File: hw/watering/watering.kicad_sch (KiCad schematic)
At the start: 8 parts, among them J2 USB_C_Receptacle

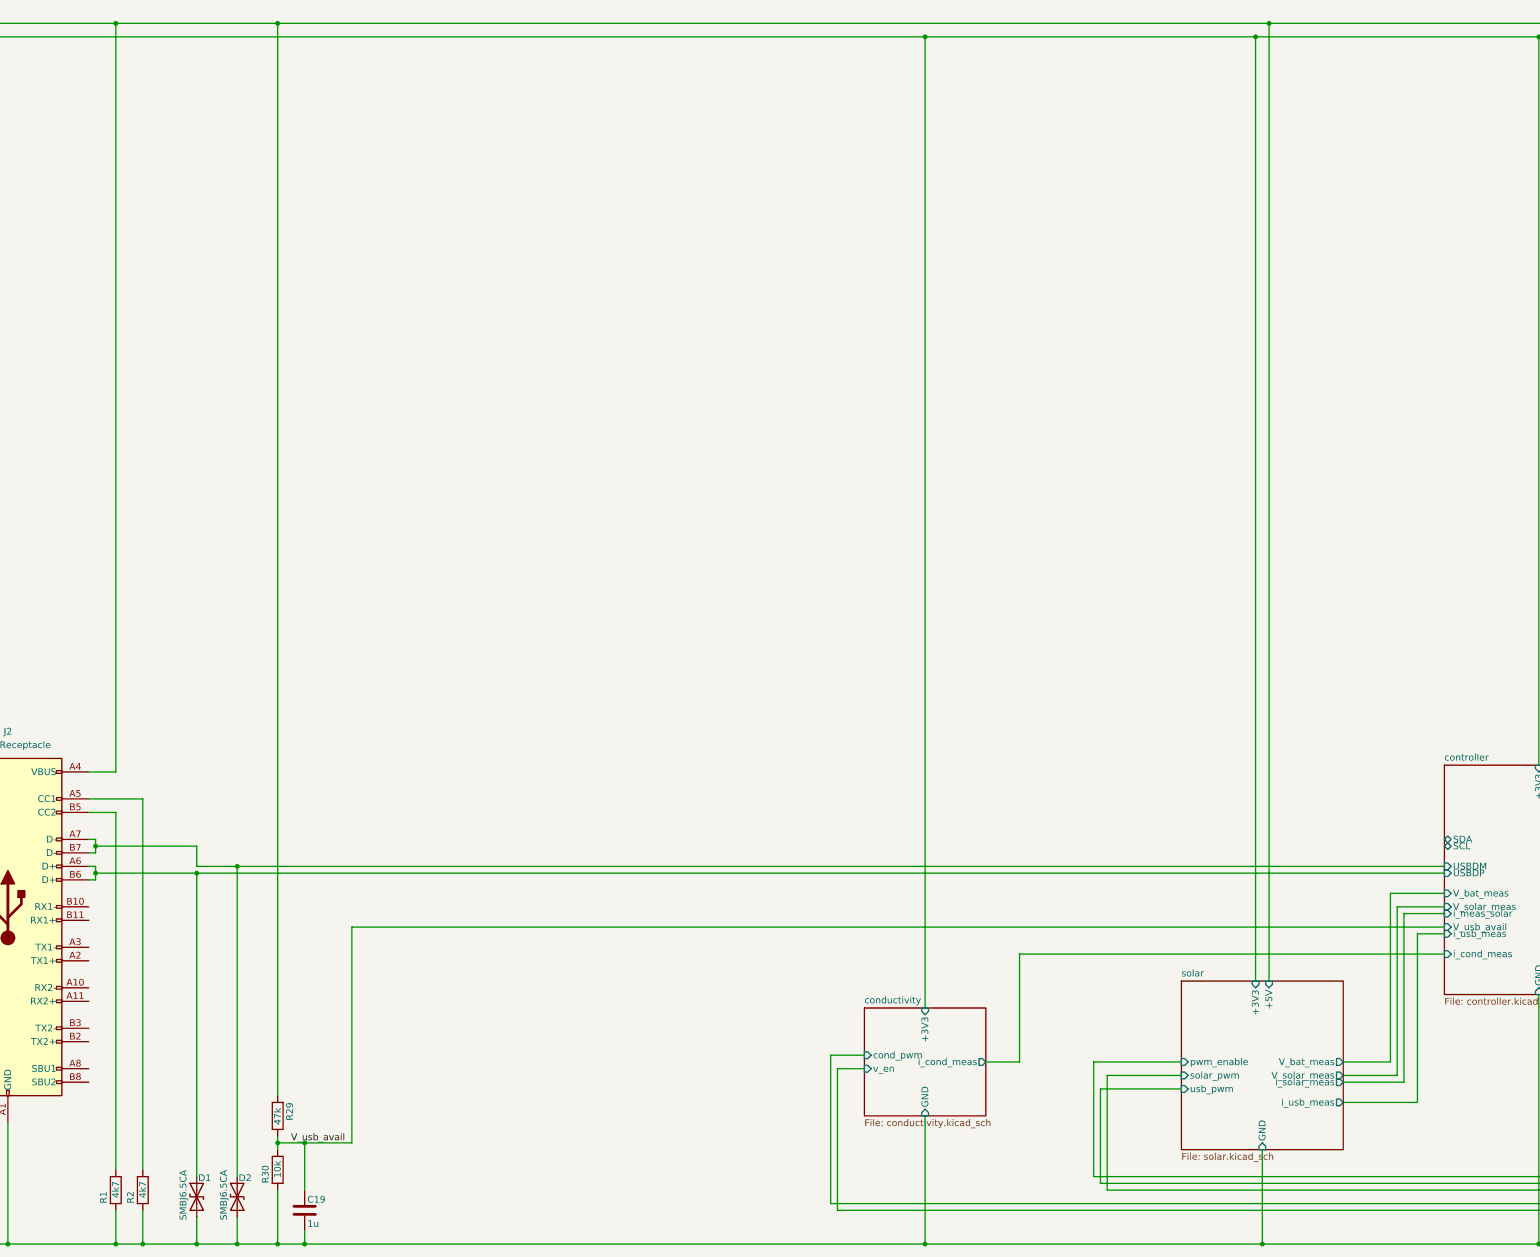
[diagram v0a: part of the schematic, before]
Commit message: more usb compliance
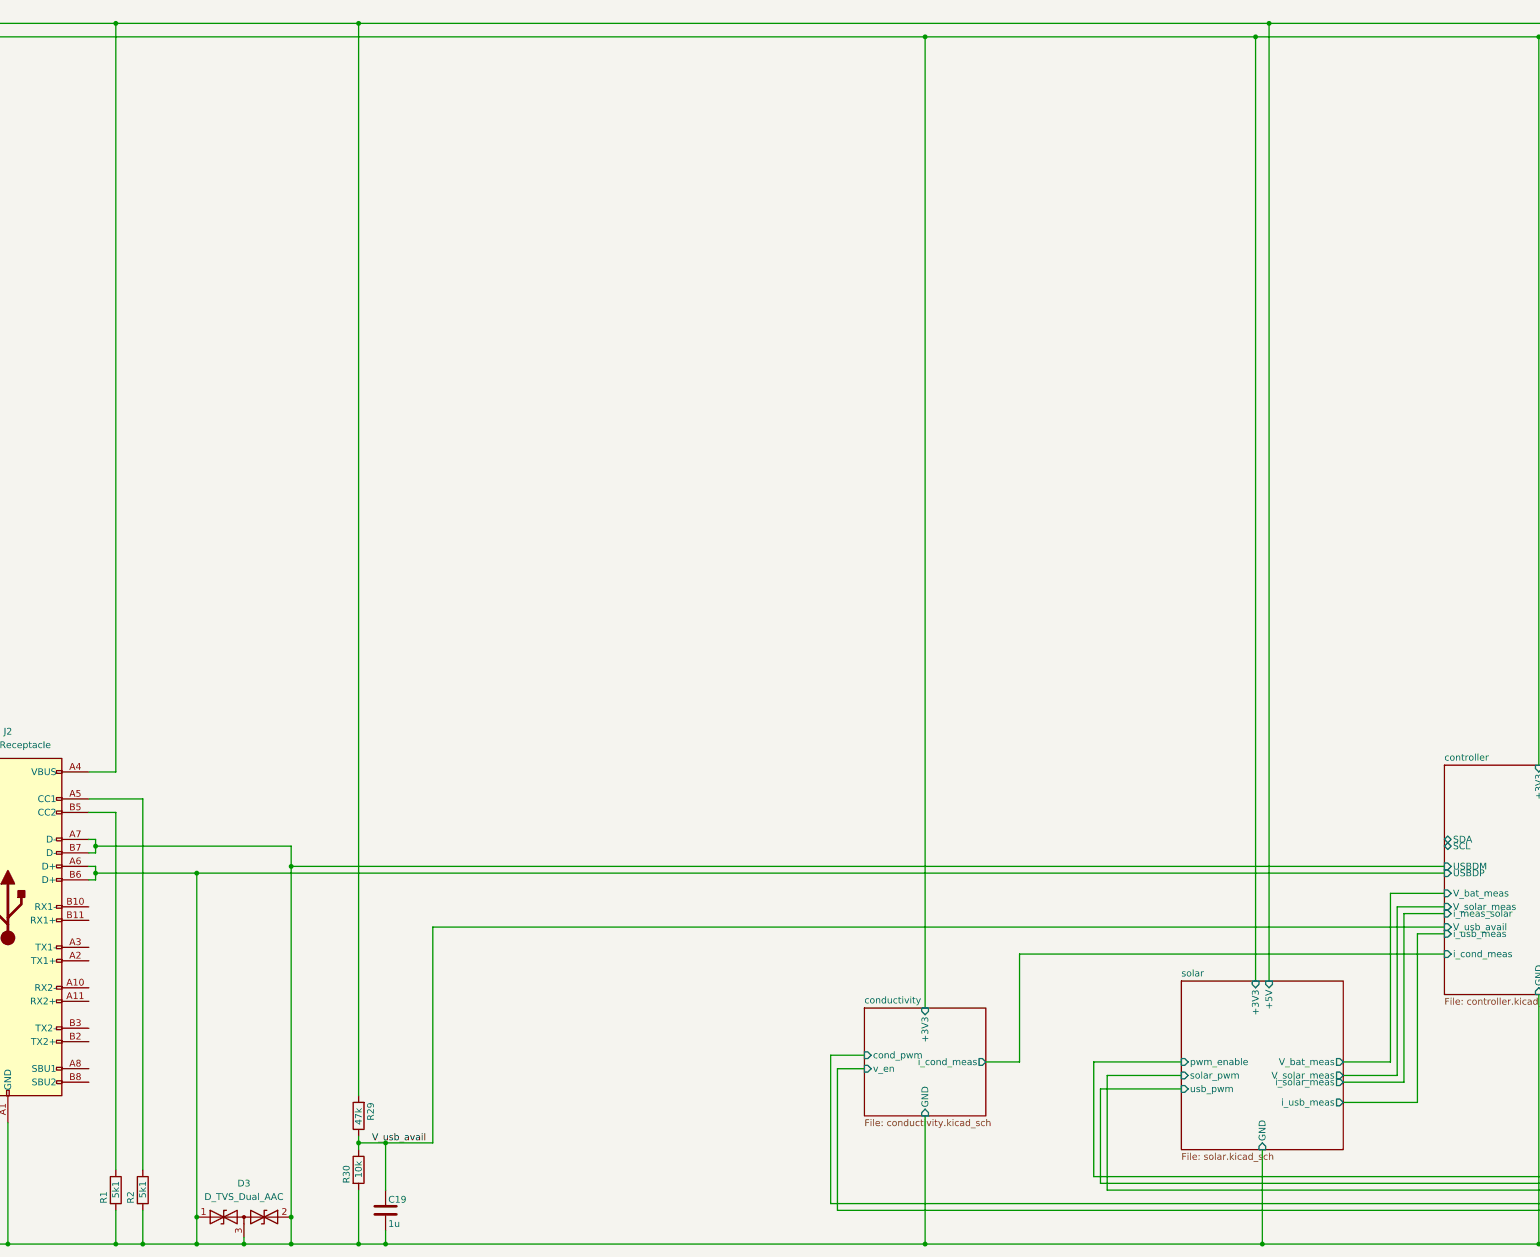
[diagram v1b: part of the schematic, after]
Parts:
- removed D1, D2: SMBJ6.5CA, Diode_SMD:D_SMB, symbol Diode:1N62xxCA
- added D3: D_TVS_Dual_AAC, symbol Device:D_TVS_Dual_AAC
- R1, R2: value 4k7 -> 5k1
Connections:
- net controller/USBDM is gone; now on net GND: J2.A7 (D-), J2.B7 (D-)
- net controller/USBDP is gone; now on net GND: J2.A6 (D+), J2.B6 (D+)
- net GND: now also D3.1 (A1), D3.2 (A2), D3.3 (common)
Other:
- moved on the sheet: C19, R29, R30

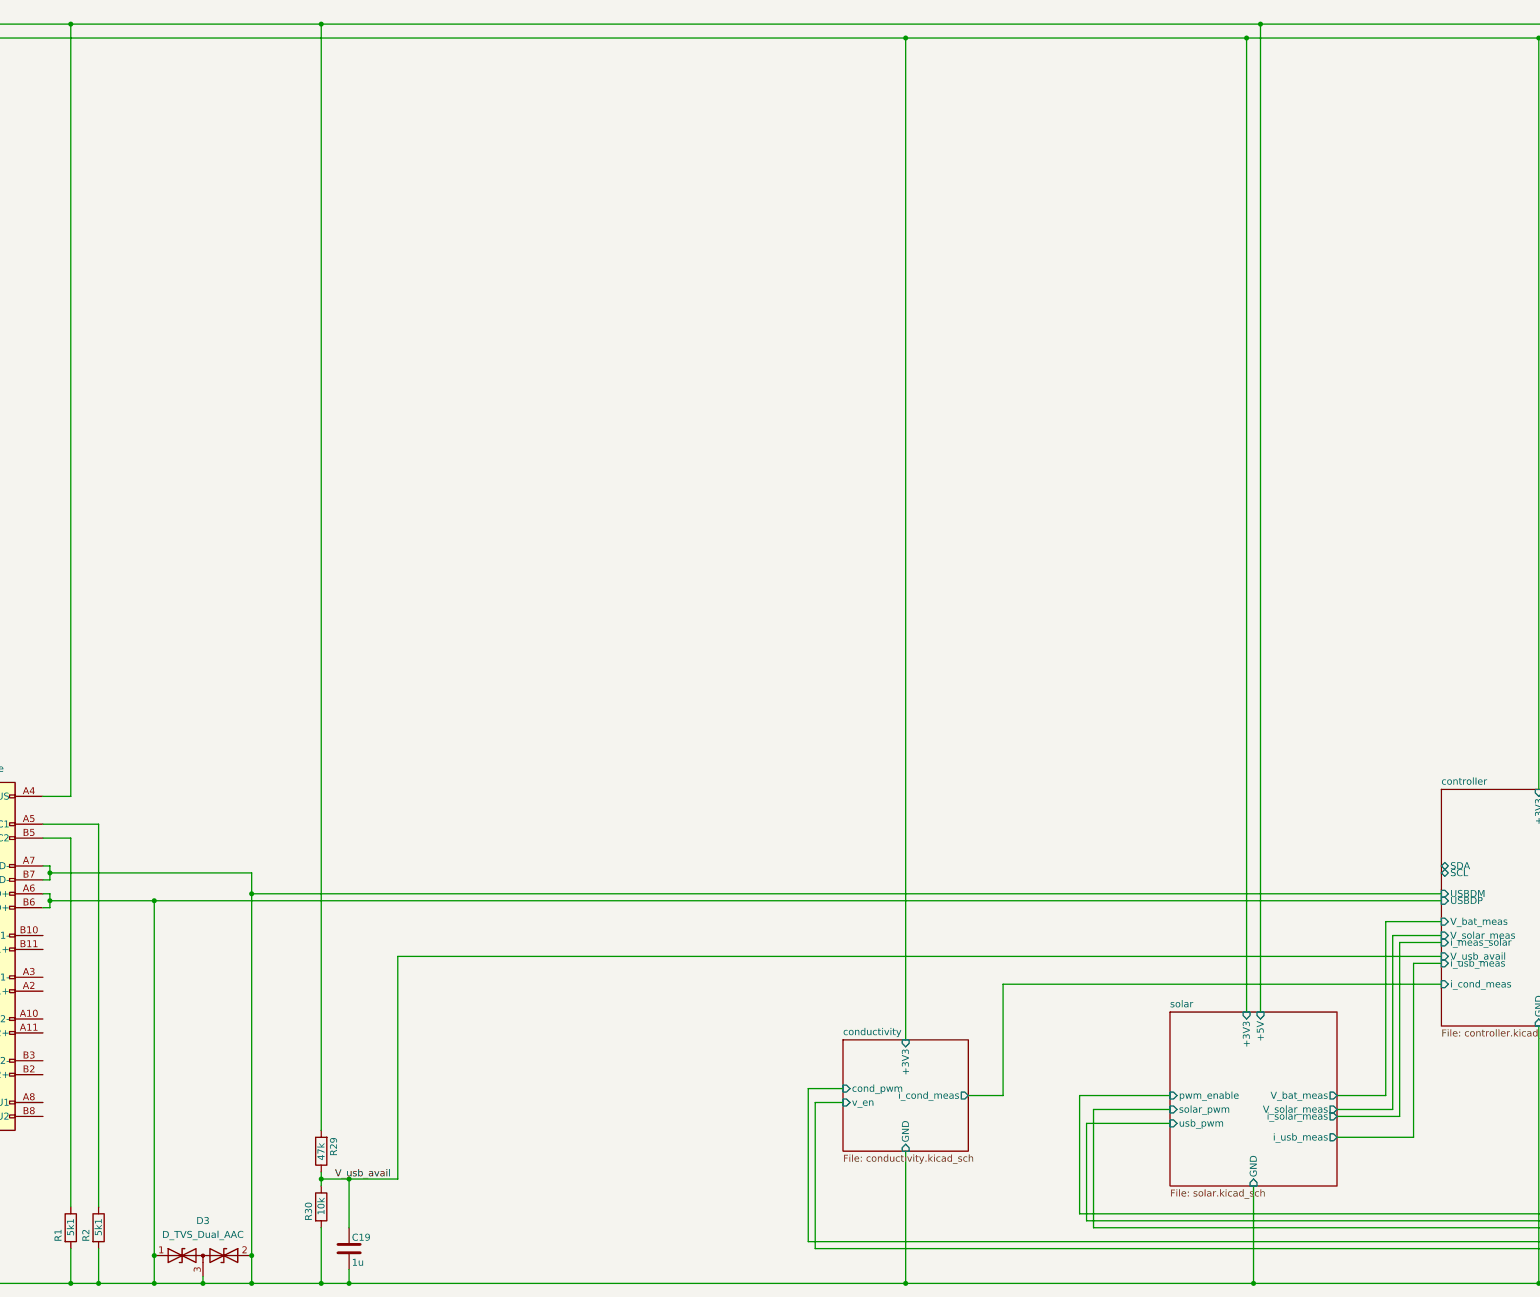
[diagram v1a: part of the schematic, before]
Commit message: - updated bom - updated dorabo connector footprint - added some stitching vias
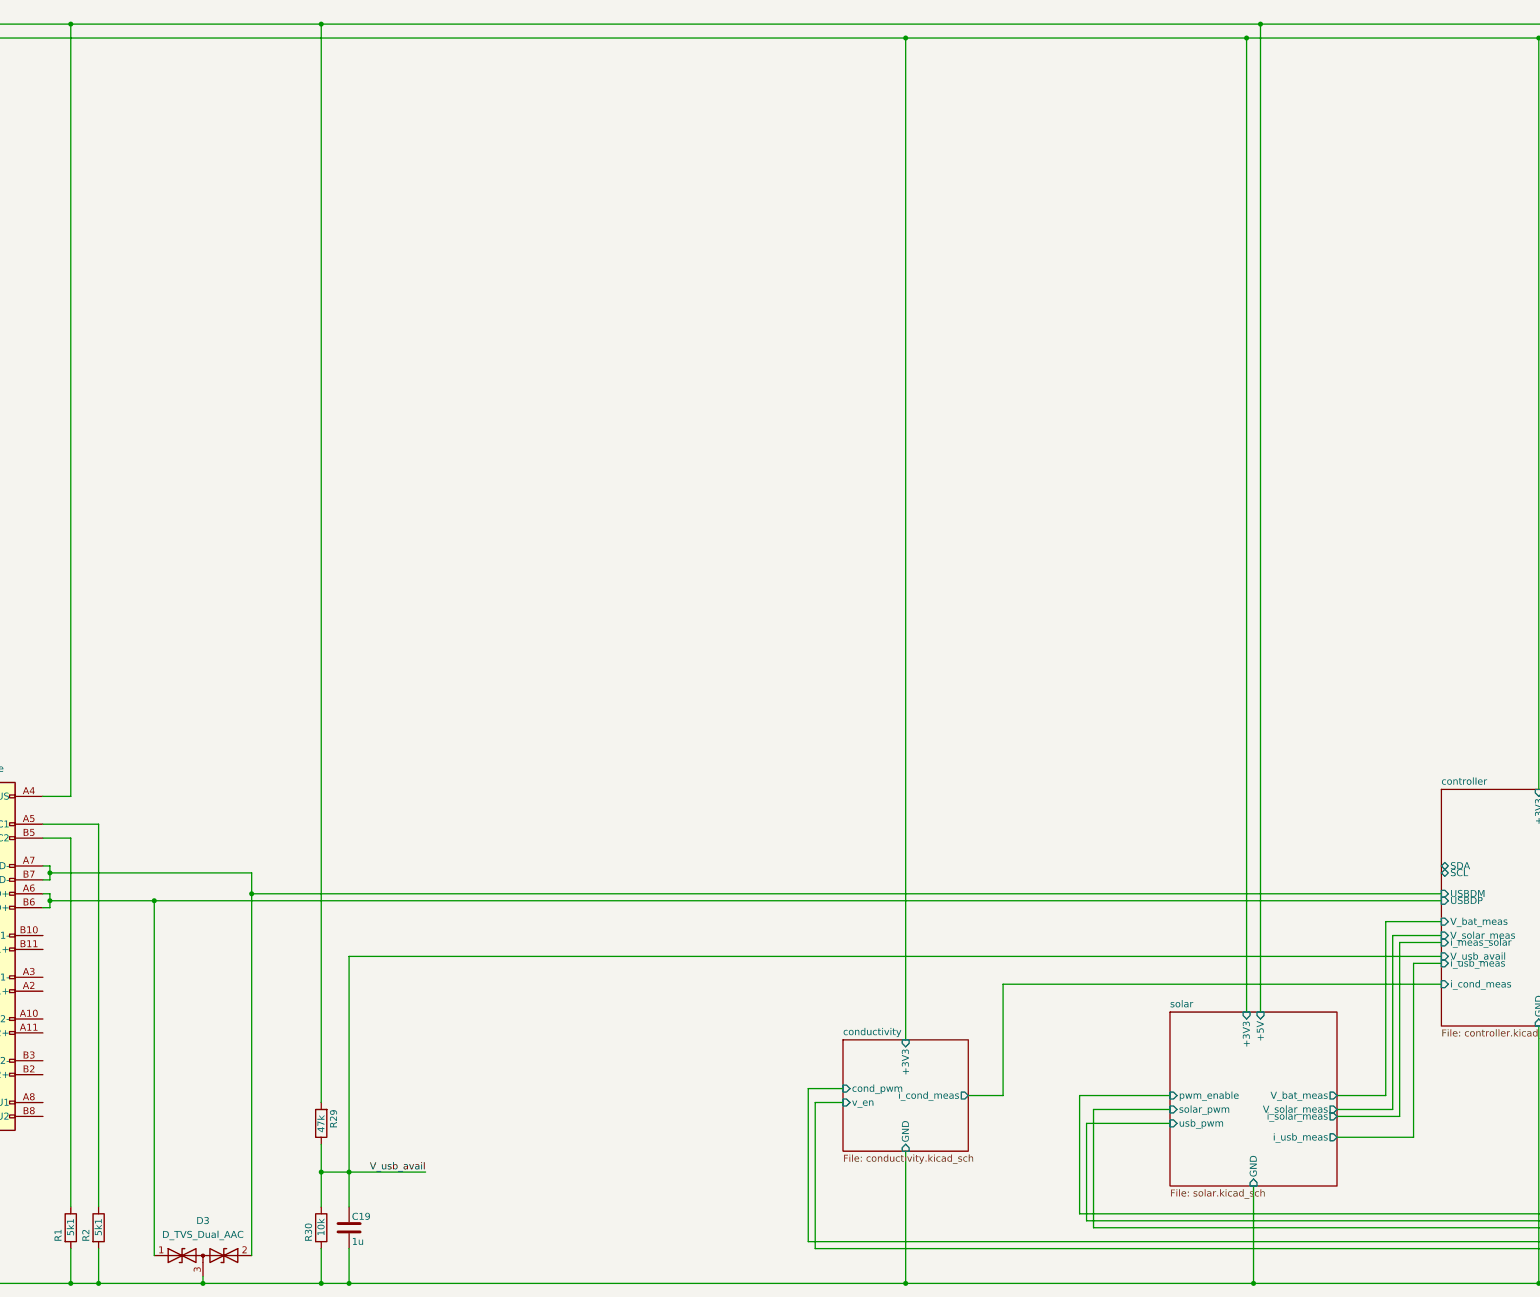
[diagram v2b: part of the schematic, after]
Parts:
- D3: footprint (none) -> Package_TO_SOT_SMD:TSOT-23
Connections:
- net GND: no longer D3.1 (A1), D3.2 (A2), J2.A6 (D+), J2.A7 (D-), J2.B6 (D+), J2.B7 (D-)
- new net controller/USBDM: D3.2 (A2), J2.A7 (D-), J2.B7 (D-)
- new net controller/USBDP: D3.1 (A1), J2.A6 (D+), J2.B6 (D+)
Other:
- moved on the sheet: C19, R29, R30
